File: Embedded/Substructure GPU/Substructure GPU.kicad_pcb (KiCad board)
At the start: 4 copper layers, 60 x 35 mm, 35 parts, among them J1 10171746-00021LF, J11 Substructure Power, J13 MicroSD, J2 HUB75 Right, J3 Display Power, J4 HUB75 Left, SW2 RST, U2 74HC245D_653, U3 74HC245D_653, U5 Substructure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

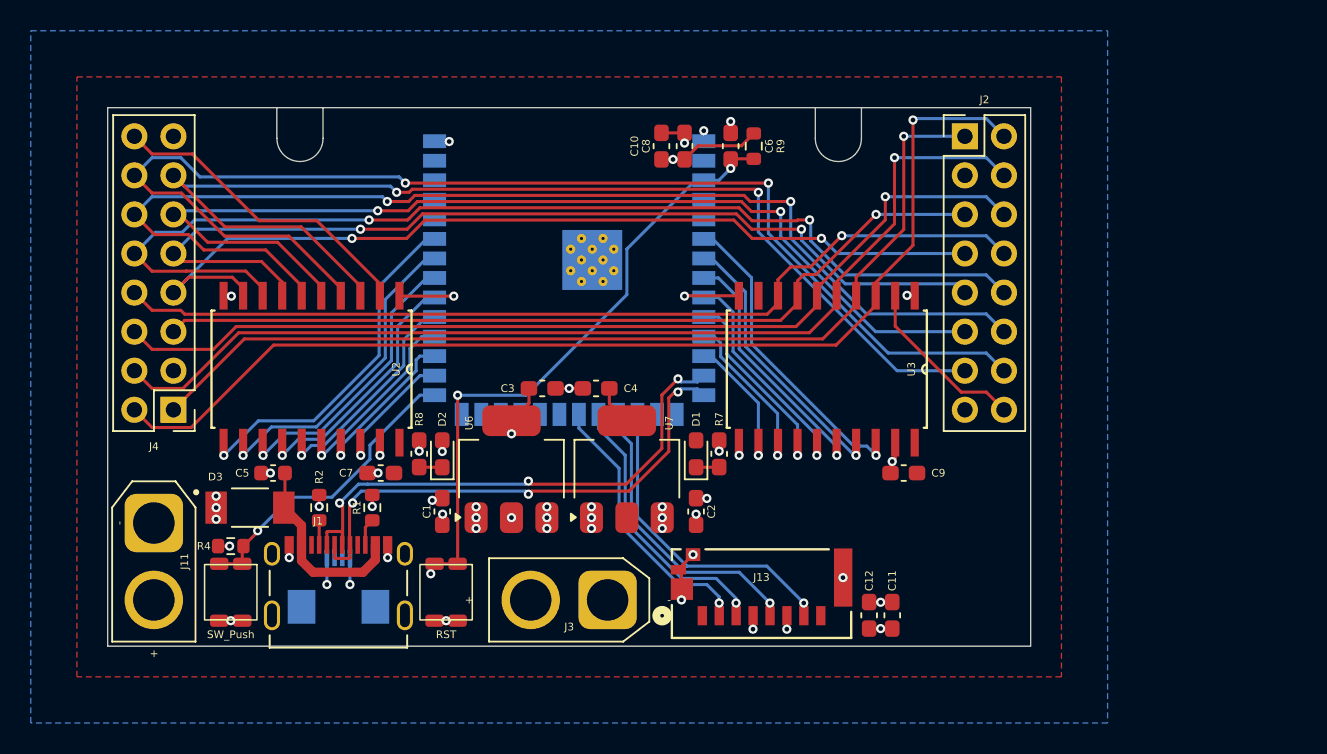
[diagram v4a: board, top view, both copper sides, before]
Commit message: Added New Routing (Improved board space & signal noise)
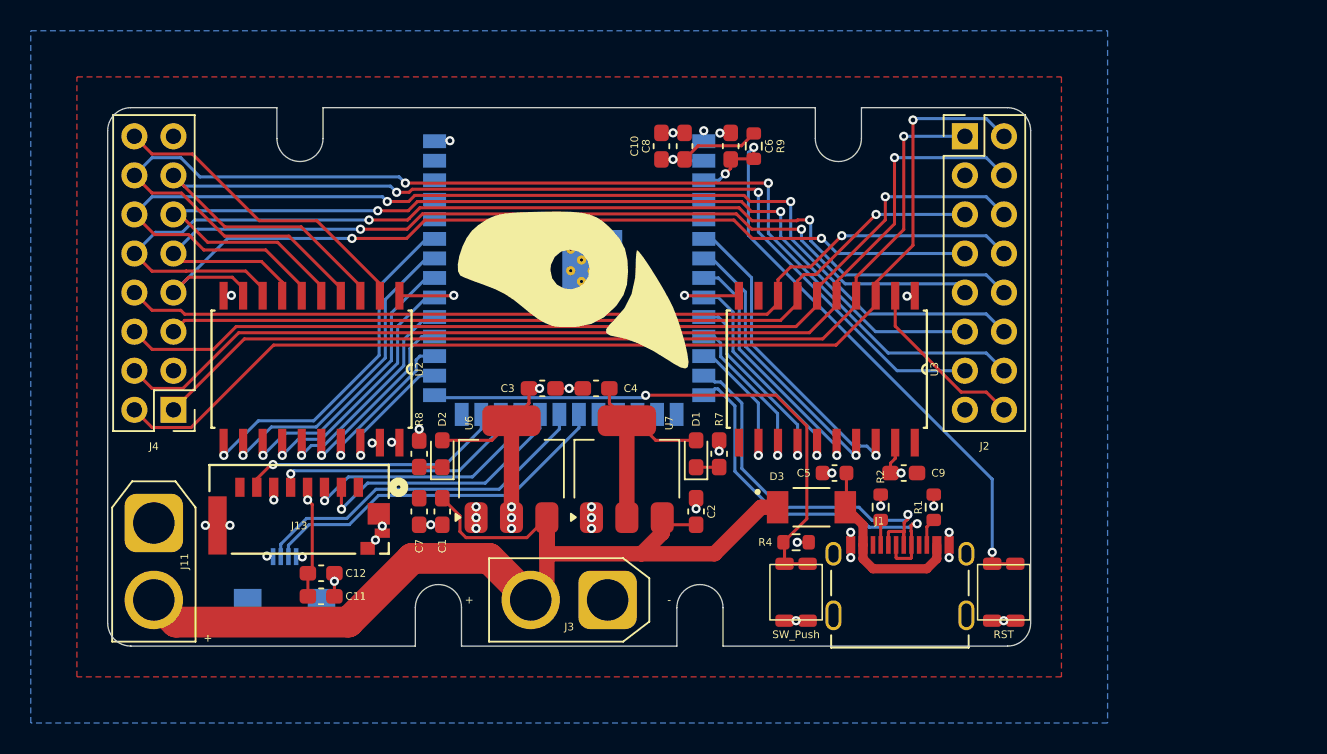
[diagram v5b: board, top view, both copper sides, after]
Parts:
- added G***: LOGO, LOGO, F.Cu at (95.2, 52.0)
- moved C11 37.1 mm to (78.9, 71.8), turned to 0 degrees
- moved R4 36.8 mm to (109.8, 68.2), turned to 180 degrees
- moved BootSW1 36.8 mm to (109.8, 71.5)
- moved D3 36.5 mm to (110.8, 66.0)
- moved R1 36.5 mm to (118.7, 66.0)
- moved R2 36.5 mm to (115.2, 66.0)
- moved C5 36.5 mm to (112.2, 63.8)
- moved J1 36.5 mm to (116.5, 73.0)
- moved SW2 36.2 mm to (123.2, 71.5)
- moved C12 35.7 mm to (78.9, 70.3), turned to 0 degrees
- moved J13 31.2 mm to (77.5, 64.7), turned to 0 degrees
- moved C7 3.54 mm to (85.2, 66.2), turned to -90 degrees
- moved U5 3.50 mm to (76.5, 69.8)
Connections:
- ESP1 pad 17: SD SPI MISO -> unconnected-(ESP1-GPIO9/TOUCH9/ADC1_CH8/FSPIHD/SUBSPIHD-Pad17)
- ESP1 pad 18: SD SPI CLK -> unconnected-(ESP1-GPIO10/TOUCH10/ADC1_CH9/FSPICS0/FSPIIO4/SUBSPICS0-Pad18)
- ESP1 pad 19: SD SPI MOSI -> unconnected-(ESP1-GPIO11/TOUCH11/ADC2_CH0/FSPID/FSPIIO5/SUBSPID-Pad19)
- ESP1 pad 20: SD SPI CS -> Power UART TX
- ESP1 pad 21: unconnected-(ESP1-GPIO13/TOUCH13/ADC2_CH2/FSPIQ/FSPIIO7/SUBSPIQ-Pad21) -> Power UART RX
- ESP1 pad 22: unconnected-(ESP1-GPIO14/TOUCH14/ADC2_CH3/FSPIWP/FSPIDQS/SUBSPIWP-Pad22) -> SD SPI CS
- ESP1 pad 23: unconnected-(ESP1-GPIO21-Pad23) -> SD SPI MOSI
- ESP1 pad 24: unconnected-(ESP1-GPIO47/SPICLK_P/SUBSPICLK_P_DIFF-Pad24) -> SD SPI CLK
- ESP1 pad 25: unconnected-(ESP1-GPIO48/SPICLK_N/SUBSPICLK_N_DIFF-Pad25) -> SD SPI MISO
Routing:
- net +RAWVS: track 54.5 -> 122.6 mm, vias 11 -> 0
- net Power UART TX: track 0.00 -> 23.7 mm
- net Power UART RX: track 0.00 -> 23.0 mm
- net +3V3: track 14.0 -> 31.4 mm
- net Net-(ESP1-GPIO0/BOOT): track 19.7 -> 36.3 mm
- net +5V: track 2.57 -> 13.7 mm, vias 0 -> 1
- net Main USB -: track 35.0 -> 24.8 mm, vias 3 -> 1
- net Main USB +: track 33.9 -> 24.8 mm, vias 3 -> 1
- net SD SPI MISO: track 20.6 -> 17.4 mm
- net GND: track 42.2 -> 39.2 mm, vias 36 -> 38
- net SD SPI CLK: track 19.3 -> 16.7 mm
- net SD SPI MOSI: track 18.1 -> 16.5 mm
- net unconnected-(U3-B7-Pad11): track 0.83 -> 0.00 mm, vias 1 -> 0
- net Net-(ESP1-EN): track 40.9 -> 40.2 mm
- net SD SPI CS: track 17.9 -> 17.4 mm
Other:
- outline, holes or cut-outs redrawn
- board text added: "Your A Tinkerer Harry"

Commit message: Modified Display pins (Corrected port orientation) & Added Silkscreen Data
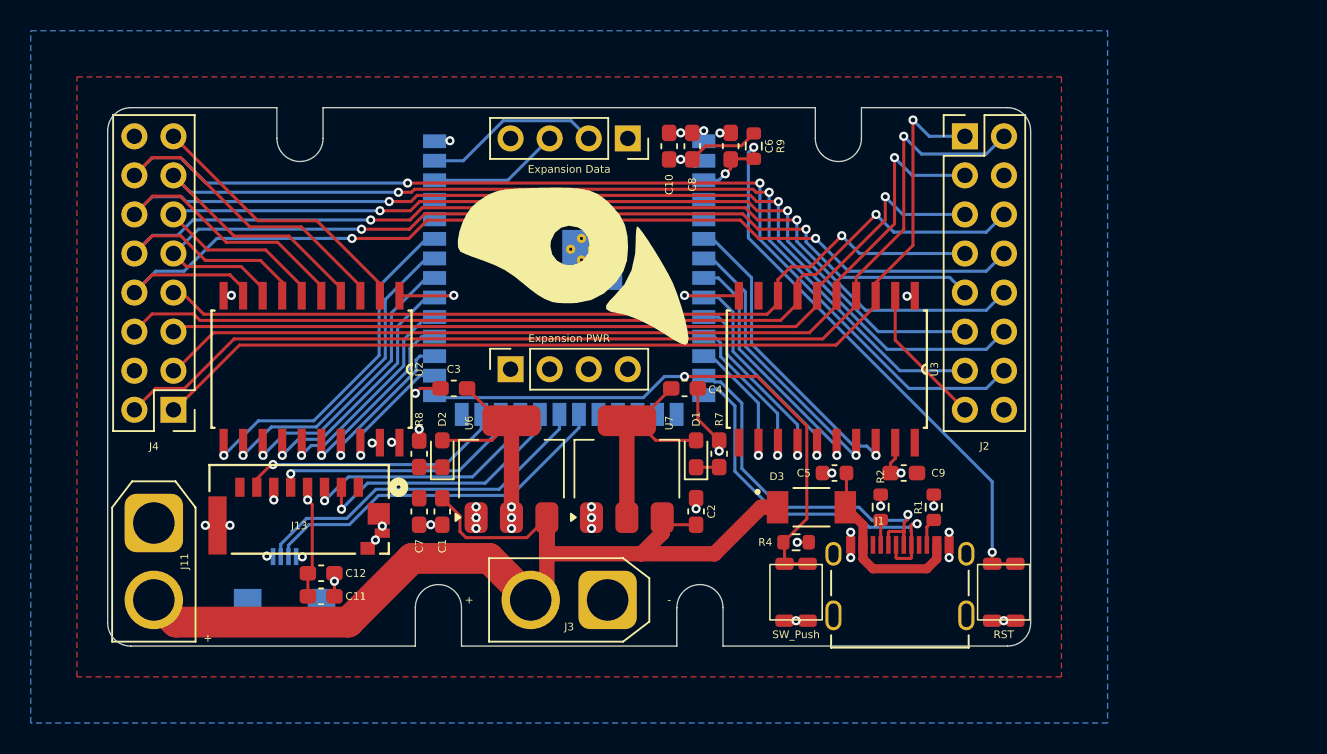
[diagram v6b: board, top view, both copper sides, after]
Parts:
- added J5: Expansion Data, Connector_PinSocket_2.54mm:PinSocket_1x04_P2.54mm_Vertical, F.Cu at (98.8, 42.0)
- added J6: Expansion PWR, Connector_PinSocket_2.54mm:PinSocket_1x04_P2.54mm_Vertical, F.Cu at (91.2, 57.0)
- moved C3 5.75 mm to (87.5, 58.2), turned to 180 degrees
- moved C4 5.75 mm to (102.5, 58.2), turned to 0 degrees
- moved G*** 1.56 mm to (95.2, 50.4)
- moved C10 0.50 mm to (101.5, 42.5)
- moved C8 0.50 mm to (103.0, 42.5)
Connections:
- ESP1 pad 38: unconnected-(ESP1-GPIO2/TOUCH2/ADC1_CH1-Pad38) -> Expansion UART TX
- ESP1 pad 39: unconnected-(ESP1-GPIO1/TOUCH1/ADC1_CH0-Pad39) -> Expansion UART RX
- J2 pad 1: G0 -> R0
- J2 pad 10: A -> B
- J2 pad 11: D -> C
- J2 pad 12: C -> D
- J2 pad 13: LAT -> CLK
- J2 pad 14: CLK -> LAT
- J2 pad 15: GND -> OE1
- J2 pad 16: OE1 -> GND
- J2 pad 2: R0 -> G0
- J2 pad 3: GND -> B0
- J2 pad 4: B0 -> GND
- J2 pad 5: G1 -> R1
- J2 pad 6: R1 -> G1
- J2 pad 7: E -> B1
- J2 pad 8: B1 -> E
- J2 pad 9: B -> A
- J4 pad 1: G0 -> R0
- J4 pad 10: A -> B
- J4 pad 11: D -> C
- J4 pad 12: C -> D
- J4 pad 13: LAT -> CLK
- J4 pad 14: CLK -> LAT
- J4 pad 15: GND -> OE0
- J4 pad 16: OE0 -> GND
- J4 pad 2: R0 -> G0
- J4 pad 3: GND -> B0
- J4 pad 4: B0 -> GND
- J4 pad 5: G1 -> R1
- J4 pad 6: R1 -> G1
- J4 pad 7: E -> B1
- J4 pad 8: B1 -> E
- J4 pad 9: B -> A
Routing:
- net +RAWVS: track 122.6 -> 159.8 mm
- net Expansion UART RX: track 0.00 -> 11.6 mm
- net LAT: track 74.2 -> 85.1 mm
- net D: track 68.4 -> 79.1 mm
- net B: track 63.8 -> 74.0 mm
- net E: track 60.0 -> 68.7 mm
- net Expansion UART TX: track 0.00 -> 8.61 mm
- net CLK: track 81.6 -> 73.1 mm
- net C: track 75.8 -> 67.4 mm
- net A: track 70.6 -> 62.4 mm
- net G1: track 55.5 -> 61.8 mm
- net G0: track 63.4 -> 69.5 mm
- net B0: track 67.1 -> 61.1 mm
- net R1: track 63.1 -> 57.1 mm
- net R0: track 71.4 -> 65.5 mm
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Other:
- board text added: "Designation: CSFB-Substructure-GPU Model No: CSF-AAA-000 Revision: D0.0"

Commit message: Modified Asset Tags
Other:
- board text added: "Des: CSF-Substructure-GPU M/N: CSF-AAA-000 Rev: D0.0 Dat: 26.07.2025"
- board text removed: "Designation: CSFB-Substructure-GPU Model No: CSF-AAA-000 Revision: D0.0"
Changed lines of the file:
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@@
 	)
 	(gr_rect
-		(start 87.5 62)
-		(end 102.5 65)
+		(start 89.25 61.5)
+		(end 100.75 65)
 		(stroke
 			(width 0.1)
@@
 		)
 	)
-	(gr_text "Designation: CSFB-Substructure-GPU\nModel No: CSF-AAA-000\nRevision: D0.0"
-		(at 102.25 63.5 0)
+	(gr_text "Des: CSF-Substructure-GPU\nM/N: CSF-AAA-000\nRev: D0.0\nDat: 26.07.2025"
+		(at 100.5 63.25 0)
 		(layer "B.SilkS")
 		(effects
